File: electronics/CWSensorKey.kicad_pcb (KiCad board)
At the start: 2 copper layers, 37 x 30 mm, 21 parts, among them J1 Tip, J2 GND, J3 Ring, J4 Dit, J5 Dah, J6 +, J7 -, Q1 IRFML8244TRPBF, Q2 IRFML8244TRPBF, U1 AT42QT1011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

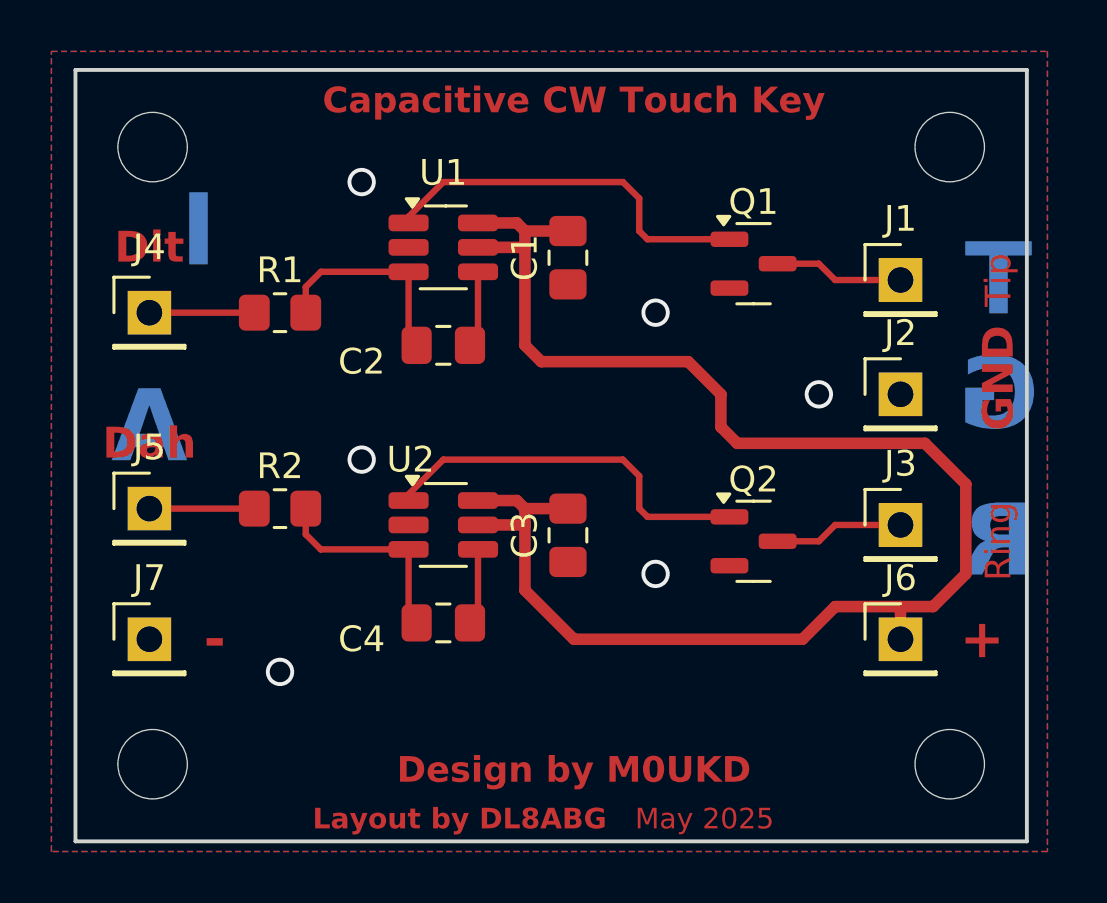
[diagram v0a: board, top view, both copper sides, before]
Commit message: Changed CW-Pad and added script for 2D generation in FreeCAD
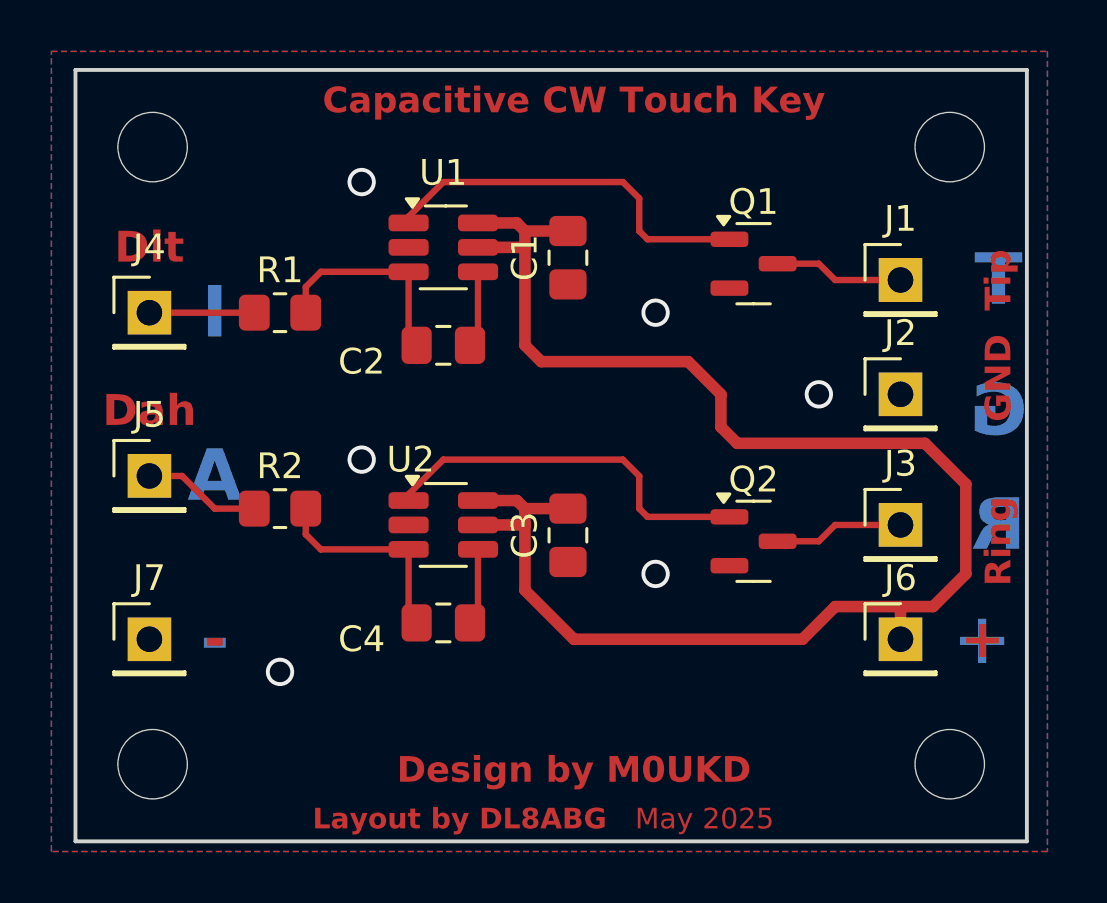
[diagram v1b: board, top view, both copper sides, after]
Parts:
- moved J5 1.27 mm to (142.9, 97.8)
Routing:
- net Net-(J5-Pin_1): track 4.08 -> 4.61 mm
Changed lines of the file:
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@@
 		(embedded_fonts no)
 		(model "${KICAD9_3DMODEL_DIR}/Connector_PinHeader_2.54mm.3dshapes/PinHeader_1x01_P2.54mm_Vertical.wrl"
+			(hide yes)
 			(offset
 				(xyz 0 0 0)
@@
 		(embedded_fonts no)
 		(model "${KICAD9_3DMODEL_DIR}/Connector_PinHeader_2.54mm.3dshapes/PinHeader_1x01_P2.54mm_Vertical.wrl"
+			(hide yes)
 			(offset
 				(xyz 0 0 0)
@@
 		(embedded_fonts no)
 		(model "${KICAD9_3DMODEL_DIR}/Connector_PinHeader_2.54mm.3dshapes/PinHeader_1x01_P2.54mm_Vertical.wrl"
+			(hide yes)
 			(offset
 				(xyz 0 0 0)
@@
 		(embedded_fonts no)
 		(model "${KICAD9_3DMODEL_DIR}/Connector_PinHeader_2.54mm.3dshapes/PinHeader_1x01_P2.54mm_Vertical.wrl"
+			(hide yes)
 			(offset
 				(xyz 0 0 0)
@@
 		(embedded_fonts no)
 		(model "${KICAD9_3DMODEL_DIR}/Connector_PinHeader_2.54mm.3dshapes/PinHeader_1x01_P2.54mm_Vertical.wrl"
+			(hide yes)
 			(offset
 				(xyz 0 0 0)
@@
 		(embedded_fonts no)
 		(model "${KICAD9_3DMODEL_DIR}/Connector_PinHeader_2.54mm.3dshapes/PinHeader_1x01_P2.54mm_Vertical.wrl"
+			(hide yes)
 			(offset
 				(xyz 0 0 0)
@@
 	(footprint "Connector_PinHeader_2.54mm:PinHeader_1x01_P2.54mm_Vertical"
 		(layer "F.Cu")
-		(at 142.875 99.06)
+		(at 142.875 97.79)
 		(descr "Through hole straight pin header, 1x01, 2.54mm pitch, single row")
 		(tags "Through hole pin header THT 1x01 2.54mm single row")
@@
 		(embedded_fonts no)
 		(model "${KICAD9_3DMODEL_DIR}/Connector_PinHeader_2.54mm.3dshapes/PinHeader_1x01_P2.54mm_Vertical.wrl"
+			(hide yes)
 			(offset
 				(xyz 0 0 0)
@@
 			(font
 				(size 1 1)
-				(thickness 0.15)
+				(thickness 0.2)
+				(bold yes)
 			)
 		)
@@
 			(font
 				(size 1 1)
-				(thickness 0.15)
+				(thickness 0.2)
+				(bold yes)
 			)
 		)
 	)
 	(gr_text "Dah"
-		(at 142.875 96.52 0)
+		(at 142.875 95.25 0)
 		(layer "F.Cu")
 		(effects
@@
 		(effects
 			(font
-				(size 1.2 1.2)
+				(size 1 1)
 				(thickness 0.2)
 				(bold yes)
@@
 	)
 	(gr_text "A"
-		(at 142.875 95.885 0)
+		(at 145.415 97.79 0)
 		(layer "B.Cu")
 		(effects
 			(font
-				(size 2.8 2.8)
+				(size 2 2)
+				(thickness 0.3)
+				(bold yes)
+			)
+			(justify mirror)
+		)
+	)
+	(gr_text "-"
+		(at 145.415 104.14 0)
+		(layer "B.Cu")
+		(effects
+			(font
+				(size 2 2)
 				(thickness 0.3)
 				(bold yes)
@@
 	)
 	(gr_text "R"
-		(at 175.895 100.33 0)
+		(at 175.895 99.695 0)
 		(layer "B.Cu")
 		(effects
 			(font
-				(size 2.8 2.8)
+				(size 2 2)
 				(thickness 0.3)
 				(bold yes)
@@
 	)
 	(gr_text "I"
-		(at 144.78 88.265 0)
+		(at 145.415 91.44 0)
+		(layer "B.Cu")
+		(effects
+			(font
+				(size 2 2)
+				(thickness 0.3)
+				(bold yes)
+			)
+			(justify mirror)
+		)
+	)
+	(gr_text "+"
+		(at 175.26 104.14 0)
 		(layer "B.Cu")
 		(effects
 			(font
-				(size 2.8 2.8)
+				(size 2 2)
 				(thickness 0.3)
 				(bold yes)
@@
 	)
 	(gr_text "G"
-		(at 175.895 94.615 0)
+		(at 175.895 95.25 0)
 		(layer "B.Cu")
 		(effects
 			(font
-				(size 2.8 2.8)
+				(size 2 2)
 				(thickness 0.3)
 				(bold yes)
@@
 		(effects
 			(font
-				(size 2.8 2.8)
+				(size 2 2)
 				(thickness 0.3)
 				(bold yes)
@@
 	)
 	(segment
-		(start 142.875 99.06)
+		(start 145.415 99.06)
 		(end 146.955 99.06)
 		(width 0.25)
 		(layer "F.Cu")
+		(net 10)
+	)
+	(segment
+		(start 144.145 97.79)
+		(end 145.415 99.06)
+		(width 0.25)
+		(layer "F.Cu")
+		(net 10)
+	)
+	(segment
+		(start 142.875 97.79)
+		(end 144.145 97.79)
+		(width 0.25)
+		(layer "F.Cu")
